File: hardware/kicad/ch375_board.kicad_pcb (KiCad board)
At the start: 2 copper layers, 100 x 100 mm, 14 parts, among them IC1 ATF22V10C, IC2 ATF22V10C, J1 Conn_02x32_Odd_Even, J2 Conn_02x08_Odd_Even, U1 AS6C4008-55PCN, U2 AS6C4008-55PCN, U3 74HCT161, U4 74LS283

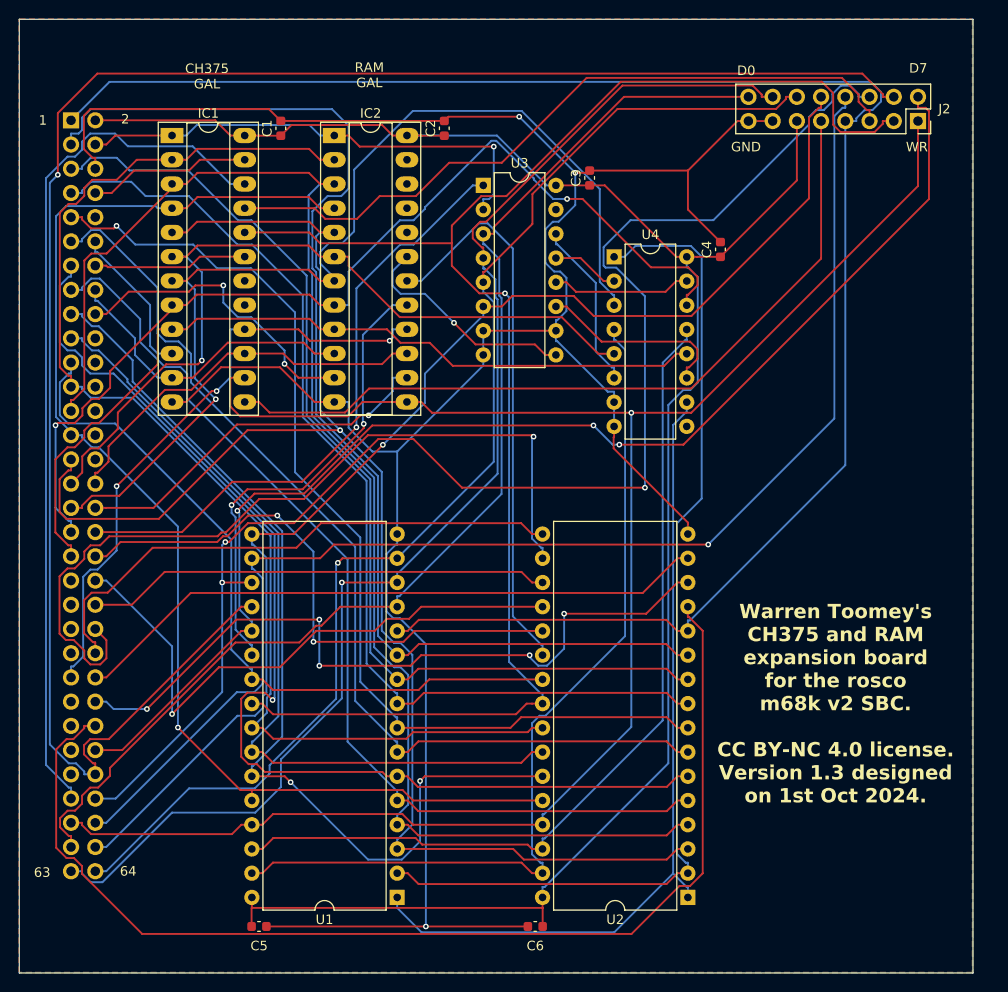
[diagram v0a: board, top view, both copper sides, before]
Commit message: hardware: Updated the PCB design now that I actually understand how to do autovector interrupts!
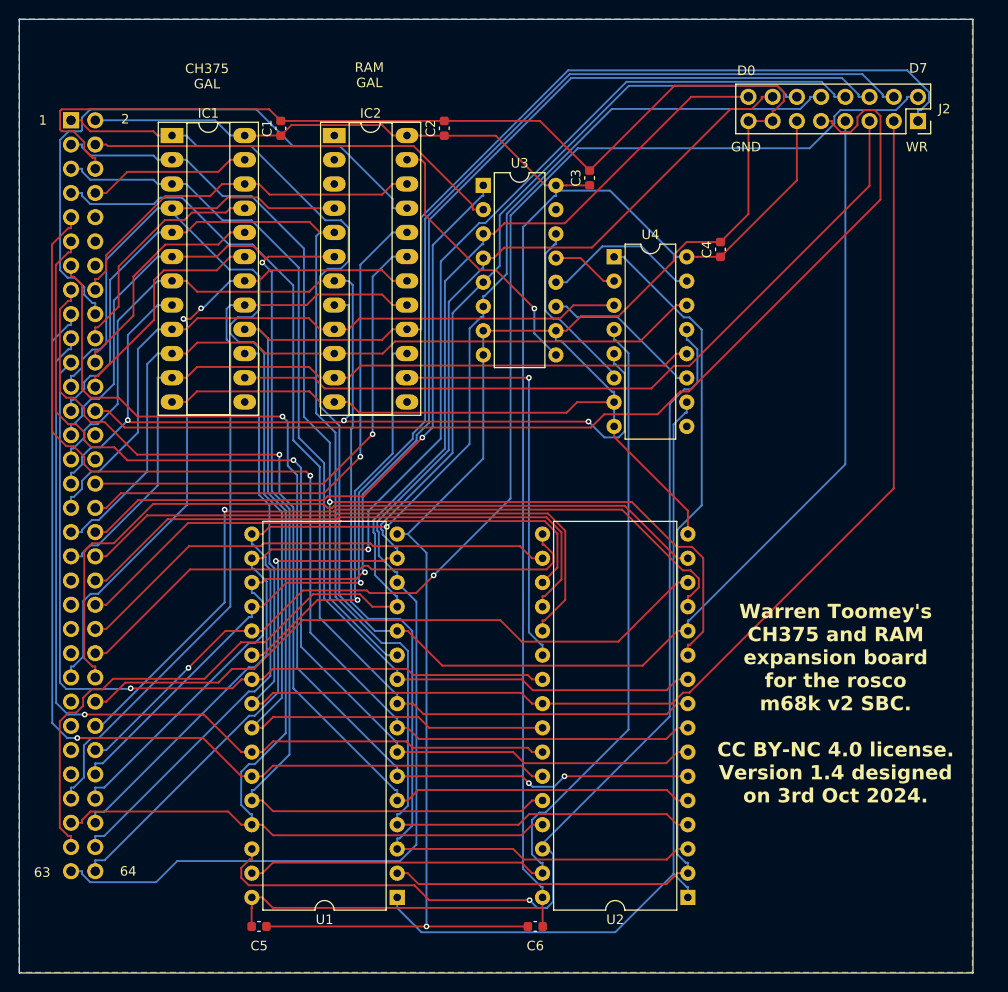
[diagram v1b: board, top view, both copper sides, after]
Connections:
- IC1 pad 1: CLK -> A1
- IC1 pad 10: VMA -> A18
- IC1 pad 11: IOSEL -> A19
- IC1 pad 13: INT -> unconnected-(IC1-I13-Pad13)
- IC1 pad 14: R~{W} -> ~{CHCS}
- IC1 pad 15: LDS -> W~{R}
- IC1 pad 16: AS -> R~{W}
- IC1 pad 17: unconnected-(IC1-I04-Pad17) -> DTACK
- IC1 pad 18: unconnected-(IC1-IO5-Pad18) -> AS
- IC1 pad 19: IRQ3 -> FC2
- IC1 pad 2: A12 -> A2
- IC1 pad 20: W~{R} -> FC1
- IC1 pad 21: ~{CHCS} -> FC0
- IC1 pad 22: DTACK -> IOSEL
- IC1 pad 3: A13 -> A3
- IC1 pad 4: A14 -> A12
- IC1 pad 5: A15 -> A13
- IC1 pad 6: A16 -> A14
- IC1 pad 7: A17 -> A15
- IC1 pad 8: A18 -> A16
- IC1 pad 9: A19 -> A17
- IC2 pad 1: CLK -> unconnected-(IC2-I1/CLK-Pad1)
- IC2 pad 10: IOSEL -> A18
- IC2 pad 11: EXPSEL -> A19
- IC2 pad 13: R~{W} -> unconnected-(IC2-I13-Pad13)
- IC2 pad 14: UDS -> ~{ERAM1}
- IC2 pad 15: LDS -> ~{ORAM1}
- IC2 pad 16: AS -> R~{W}
- IC2 pad 17: ~{ORAM1} -> DTACK
- IC2 pad 18: ~{ERAM1} -> AS
- IC2 pad 19: ~{BASESEL} -> LDS
- IC2 pad 2: A12 -> unconnected-(IC2-I2-Pad2)
- IC2 pad 20: unconnected-(IC2-IO7-Pad20) -> UDS
- IC2 pad 21: unconnected-(IC2-IO8-Pad21) -> EXPSEL
- IC2 pad 22: unconnected-(IC2-IO9-Pad22) -> IOSEL
- IC2 pad 23: unconnected-(IC2-IO10-Pad23) -> ~{BASESEL}
- IC2 pad 3: A13 -> unconnected-(IC2-I3-Pad3)
- IC2 pad 4: A14 -> A12
- IC2 pad 5: A15 -> A13
- IC2 pad 6: A16 -> A14
- IC2 pad 7: A17 -> A15
- IC2 pad 8: A18 -> A16
- IC2 pad 9: A19 -> A17
- J2 pad 9: INT -> IRQ5
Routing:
- net IRQ5: track 0.00 -> 110.3 mm
- net INT: track 82.0 -> 0.00 mm
- net D6: track 190.6 -> 135.2 mm
- net A17: track 112.4 -> 73.0 mm, vias 1 -> 0
- net GND: track 274.9 -> 311.1 mm, vias 3 -> 1
- net D12: track 86.3 -> 51.3 mm, vias 1 -> 0
- net D8: track 118.9 -> 85.1 mm, vias 0 -> 1
- net EXPSEL: track 32.2 -> 63.8 mm, vias 2 -> 0
- net FC0: track 0.00 -> 24.5 mm
- net FC2: track 0.00 -> 24.4 mm
- net FC1: track 0.00 -> 24.4 mm
- net A18: track 106.2 -> 82.1 mm, vias 2 -> 0
- net A15: track 160.7 -> 140.6 mm, vias 1 -> 0
- net UDS: track 39.2 -> 56.4 mm
- net IRQ3: track 16.2 -> 0.00 mm
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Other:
- board text added: "Warren Toomey's CH375 and RAM expansion board for the rosco m68k v2 SBC. CC BY-NC 4.0 license. Version 1.4 designed on 3rd Oct 2024."
- board text removed: "Warren Toomey's CH375 and RAM expansion board for the rosco m68k v2 SBC. CC BY-NC 4.0 license. Version 1.3 designed on 1st Oct 2024."
